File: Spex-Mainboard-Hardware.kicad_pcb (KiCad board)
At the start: 4 copper layers, 82 x 84.7 mm, 118 parts, among them P1 USB_OTG, P13 CONN_01X02, P14 CONN_01X02, P2 SWD Header, P3 CONN_01X04, P4 CONN_01X04, P5 CONN_01X04, P6 CONN_01X04, P7 CONN_01X02, P8 CONN_01X02, P9 CONN_01X02, Q105 Si3407DV, Q106 Q_PNP_BEC, Q3 BSS215PH6327, Q4 Si5468DC, Q5 Si5468DC, Q6 Si5468DC, SW1 SW_PUSH, SW2 SW_PUSH, U1 MKL02Z32VFG4, U10 LM4030, U105 TPS563200, U108 TPS563200, U12 ST1480ABDR, U13 SCHA4B0419, U14 AT45DB641E, U2 NUP2201MR6, U3 MK20DX256VLH7, U4 NUP2201MR6, U5 NUP2201MR6, U6 MMQA6V2T1G, U7 MCP9808T, U8 BME280, U9 LSM9DS1, Y1 Crystal

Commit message: added images
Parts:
- moved C105 99.8 mm to (174.7, 75.8)
- moved C11 99.8 mm to (150.7, 118.3)
- moved C114 99.8 mm to (166.1, 76.0)
- moved C119 99.8 mm to (151.8, 71.8)
- moved C12 99.8 mm to (154.0, 127.9)
- moved C120 99.8 mm to (155.5, 77.4)
- moved C121 99.8 mm to (163.9, 64.4)
- moved C123 99.8 mm to (144.8, 69.2)
- moved C13 99.8 mm to (154.0, 121.4)
- moved C14 99.8 mm to (183.5, 61.1)
- moved C15 99.8 mm to (154.0, 123.6)
- moved C16 99.8 mm to (154.0, 125.3)
- moved C18 99.8 mm to (170.8, 123.7)
- moved C19 99.8 mm to (116.1, 111.6)
- moved C2 99.8 mm to (148.5, 107.1)
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
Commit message: small update
getting ready to order PCB's, making sure they are good to go.
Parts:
- removed P2: SWD Header, SPEX_Parts:SWD-10
- moved P9 4.60 mm to (191.3, 103.1)
- moved Q6 4.60 mm to (179.2, 104.5)
- moved R37 4.60 mm to (175.6, 105.2)
- moved P8 4.47 mm to (191.3, 94.0)
- moved R36 4.47 mm to (175.6, 96.0)
- moved Q5 4.47 mm to (179.2, 95.3)
- moved P7 4.37 mm to (191.3, 84.8)
- moved R35 4.37 mm to (175.6, 86.9)
- moved Q4 4.37 mm to (179.2, 86.2)
- moved P4 1.92 mm to (191.5, 121.2)
- moved P3 1.92 mm to (191.5, 110.1)
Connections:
- net VBatt renamed /Power Distribution/VBat
- P3 pad 2: I2C1_SDA -> I2C1_SCL
- P3 pad 3: I2C1_SCL -> I2C1_SDA
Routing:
- net Vbus_MOS_CTRL: track 23.7 -> 28.8 mm
- net Vbus: track 64.0 -> 69.0 mm
- net I2C1_SDA: track 54.8 -> 57.4 mm
- net UART2_RX: track 51.2 -> 53.4 mm
- net UART2_TX: track 50.7 -> 52.7 mm
- net 5V_MOS_CTRL: track 27.4 -> 28.7 mm
- net 3.3V_MOS_CTRL: track 34.9 -> 36.0 mm
- net GND: track 128.9 -> 129.9 mm, vias 59 -> 60
- net SPI0_SCK: track 69.7 -> 70.5 mm
- net +5V: track 62.5 -> 63.3 mm
- added copper zone on F.Cu, net VBatt
- removed copper zone on F.Cu, net /Power Distribution/VBat

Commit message: small update round 2
cleaning up PCB, adding SPI CS pullup resistors
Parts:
- added R19: 10K, Resistors_SMD:R_0603, F.Cu at (138.5, 127.1)
- added R20: 10K, Resistors_SMD:R_0603, F.Cu at (156.8, 109.6)
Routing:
- net /Power Distribution/VBat: track 0.00 -> 10.9 mm
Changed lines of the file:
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@@
 (kicad_pcb (version 4) (host pcbnew 4.0.2-stable)
   (general
-    (links 336)
+    (links 340)
     (no_connects 20)
     (area 112.379999 54.109999 194.480001 138.910001)
     (thickness 1.6)
     (drawings 4)
-    (tracks 1091)
+    (tracks 1096)
     (zones 0)
-    (modules 117)
+    (modules 119)
     (nets 119)
   )
@@
       (net 2 GND))
   )
+  (module Resistors_SMD:R_0603 (layer F.Cu)
+    (at 138.4561 127.1016)
+    (descr "Resistor SMD 0603, reflow soldering, Vishay (see dcrcw.pdf)")
+    (tags "resistor 0603")
+    (attr smd)
+    (fp_text reference R19 (at -0.623 -1.2446) (layer F.SilkS)
+      (effects (font (size 0.5 0.5) (thickness 0.125)))
+    )
+    (fp_text value 10K (at -0.6357 1.2827) (layer F.Fab)
+      (effects (font (size 0.5 0.5) (thickness 0.125)))
+    )
+    (fp_line (start -1.3 -0.8) (end 1.3 -0.8) (layer F.CrtYd) (width 0.05))
+    (fp_line (start -1.3 0.8) (end 1.3 0.8) (layer F.CrtYd) (width 0.05))
+    (fp_line (start -1.3 -0.8) (end -1.3 0.8) (layer F.CrtYd) (width 0.05))
+    (fp_line (start 1.3 -0.8) (end 1.3 0.8) (layer F.CrtYd) (width 0.05))
+    (fp_line (start 0.5 0.675) (end -0.5 0.675) (layer F.SilkS) (width 0.15))
+    (fp_line (start -0.5 -0.675) (end 0.5 -0.675) (layer F.SilkS) (width 0.15))
+    (pad 1 smd rect (at -0.75 0) (size 0.5 0.9) (layers F.Cu F.Paste F.Mask)
+      (net 1 +3V3))
+    (pad 2 smd rect (at 0.75 0) (size 0.5 0.9) (layers F.Cu F.Paste F.Mask)
+      (net 89 SPI0_CS1))
+    (model Resistors_SMD.3dshapes/R_0603.wrl
+      (at (xyz 0 0 0))
+      (scale (xyz 1 1 1))
+      (rotate (xyz 0 0 0))
+    )
+  )
+  (module Resistors_SMD:R_0603 (layer F.Cu)
+    (at 156.7942 109.5756)
+    (descr "Resistor SMD 0603, reflow soldering, Vishay (see dcrcw.pdf)")
+    (tags "resistor 0603")
+    (attr smd)
+    (fp_text reference R20 (at -0.6731 -1.1811) (layer F.SilkS)
+      (effects (font (size 0.5 0.5) (thickness 0.125)))
+    )
+    (fp_text value 10K (at -0.6223 1.2192) (layer F.Fab)
+      (effects (font (size 0.5 0.5) (thickness 0.125)))
+    )
+    (fp_line (start -1.3 -0.8) (end 1.3 -0.8) (layer F.CrtYd) (width 0.05))
+    (fp_line (start -1.3 0.8) (end 1.3 0.8) (layer F.CrtYd) (width 0.05))
+    (fp_line (start -1.3 -0.8) (end -1.3 0.8) (layer F.CrtYd) (width 0.05))
+    (fp_line (start 1.3 -0.8) (end 1.3 0.8) (layer F.CrtYd) (width 0.05))
+    (fp_line (start 0.5 0.675) (end -0.5 0.675) (layer F.SilkS) (width 0.15))
+    (fp_line (start -0.5 -0.675) (end 0.5 -0.675) (layer F.SilkS) (width 0.15))
+    (pad 1 smd rect (at -0.75 0) (size 0.5 0.9) (layers F.Cu F.Paste F.Mask)
+      (net 1 +3V3))
+    (pad 2 smd rect (at 0.75 0) (size 0.5 0.9) (layers F.Cu F.Paste F.Mask)
+      (net 90 SPI0_CS0))
+    (model Resistors_SMD.3dshapes/R_0603.wrl
+      (at (xyz 0 0 0))
+      (scale (xyz 1 1 1))
+      (rotate (xyz 0 0 0))
+    )
+  )
   (gr_line (start 112.43 54.16) (end 194.43 54.16) (angle 90) (layer Edge.Cuts) (width 0.1))
   (gr_line (start 194.43 54.16) (end 194.43 138.86) (angle 90) (layer Edge.Cuts) (width 0.1))
@@
   (segment (start 140.659699 100.30359) (end 140.603289 100.36) (width 0.2032) (layer B.Cu) (net 117))
   (segment (start 161.04859 100.30359) (end 140.659699 100.30359) (width 0.2032) (layer B.Cu) (net 117))
+  (segment (start 130.8608 67.9831) (end 132.6601 67.9831) (width 0.2032) (layer F.Cu) (net 118))
+  (segment (start 132.6601 67.9831) (end 133.18 67.4632) (width 0.2032) (layer F.Cu) (net 118))
+  (segment (start 133.18 67.4632) (end 133.18 66.11) (width 0.2032) (layer F.Cu) (net 118))
+  (segment (start 128.3339 70.51) (end 130.8608 67.9831) (width 0.2032) (layer F.Cu) (net 118))
+  (segment (start 124.88 70.51) (end 128.3339 70.51) (width 0.2032) (layer F.Cu) (net 118))
   (zone (net 2) (net_name GND) (layer B.Cu) (hatch edge 0.508)
     (connect_pads (clearance 0.25))

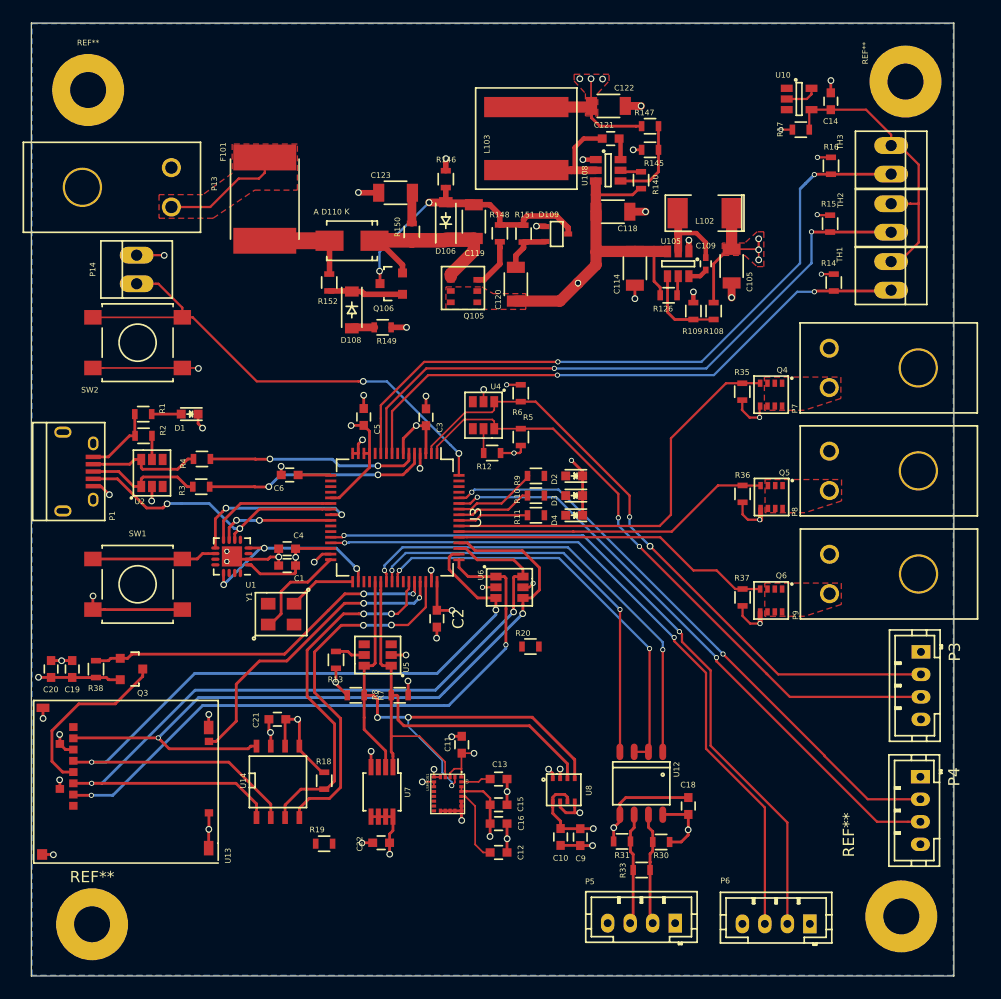
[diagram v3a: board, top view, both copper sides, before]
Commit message: fixed mounting points
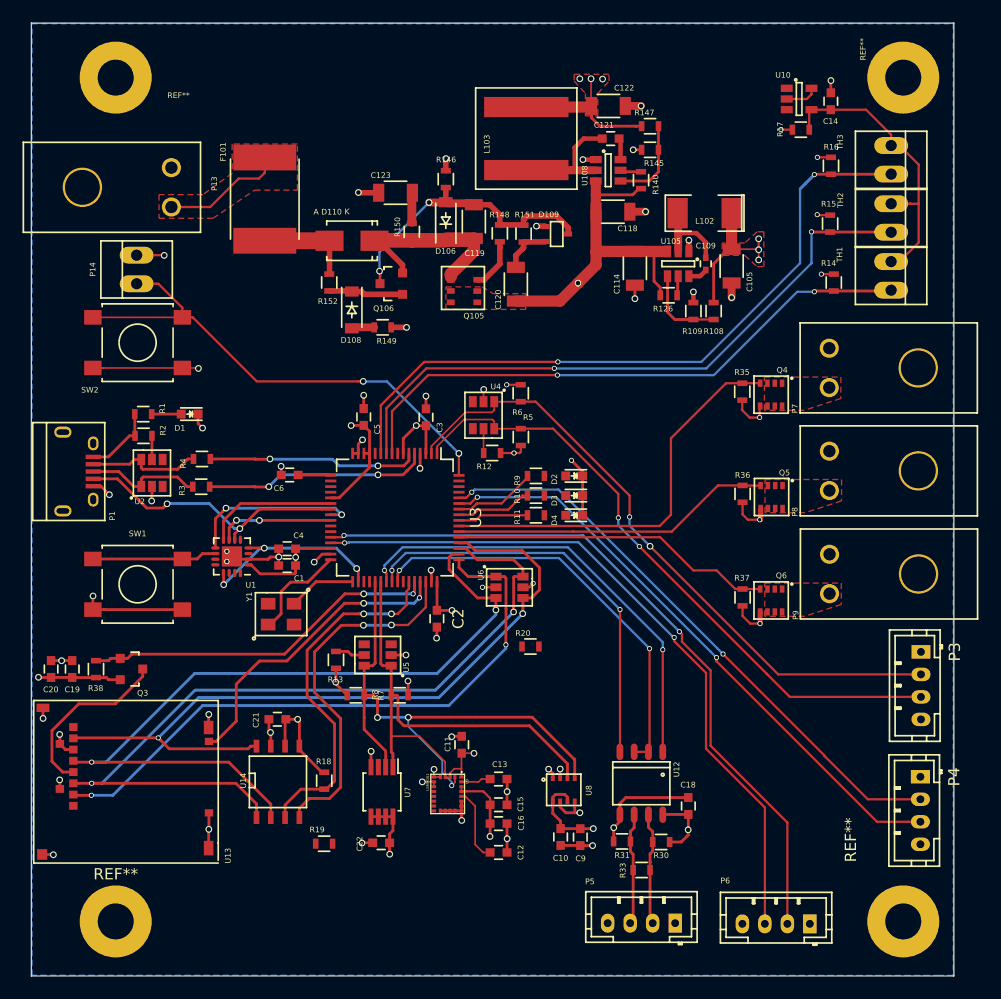
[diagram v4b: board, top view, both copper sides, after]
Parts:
- moved REF** 2.69 mm to (119.9, 59.0)
- moved REF** 2.11 mm to (119.9, 134.0)
- moved REF** 0.48 mm to (189.9, 134.0)
- moved REF** 0.40 mm to (189.9, 59.0)
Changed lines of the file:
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@@
 (kicad_pcb (version 4) (host pcbnew 4.0.2-stable)
   (general
-    (links 340)
-    (no_connects 20)
-    (area 112.379999 54.109999 194.480001 138.910001)
+    (links 324)
+    (no_connects 9)
+    (area 110.8283 54.109999 198.2903 138.910001)
     (thickness 1.6)
     (drawings 4)
@@
   )
   (setup
-    (last_trace_width 0.2032)
+    (last_trace_width 0.254)
     (user_trace_width 0.1524)
     (user_trace_width 0.2032)
@@
     (mod_text_size 1 1)
     (mod_text_width 0.15)
-    (pad_size 1.5 1.5)
-    (pad_drill 0.6)
+    (pad_size 6.4 6.4)
+    (pad_drill 3.2)
     (pad_to_mask_clearance 0)
     (aux_axis_origin 0 0)
@@
     (add_net "Net-(P1-Pad2)")
     (add_net "Net-(P1-Pad3)")
-    (add_net "Net-(P2-Pad6)")
-    (add_net "Net-(P2-Pad7)")
-    (add_net "Net-(P2-Pad8)")
-    (add_net "Net-(P2-Pad9)")
     (add_net "Net-(Q101-Pad3)")
     (add_net "Net-(Q104-Pad3)")
@@
   )
   (module Mounting_Holes:MountingHole_3.2mm_M3_Pad (layer F.Cu)
-    (at 117.83 134.26)
+    (at 119.93 134.01)
     (descr "Mounting Hole 3.2mm, M3")
     (tags "mounting hole 3.2mm m3")
@@
   )
   (module Mounting_Holes:MountingHole_3.2mm_M3_Pad (layer F.Cu)
-    (at 117.48 60.11)
+    (at 119.93 59.01)
     (descr "Mounting Hole 3.2mm, M3")
     (tags "mounting hole 3.2mm m3")
-    (fp_text reference REF** (at 0 -4.2) (layer F.SilkS)
+    (fp_text reference REF** (at 5.5841 1.5817) (layer F.SilkS)
       (effects (font (size 0.5 0.5) (thickness 0.125)))
     )
-    (fp_text value MountingHole_3.2mm_M3_Pad (at 1.302 -5.178) (layer F.Fab)
+    (fp_text value MountingHole_3.2mm_M3_Pad (at -0.0293 -4.0952) (layer F.Fab)
       (effects (font (size 0.5 0.5) (thickness 0.125)))
     )
@@
   )
   (module Mounting_Holes:MountingHole_3.2mm_M3_Pad (layer F.Cu)
-    (at 190.13 59.36)
+    (at 189.93 59.01)
     (descr "Mounting Hole 3.2mm, M3")
     (tags "mounting hole 3.2mm m3")
@@
   )
   (module Mounting_Holes:MountingHole_3.2mm_M3_Pad (layer F.Cu)
-    (at 189.755 133.56)
+    (at 189.93 134.01)
     (descr "Mounting Hole 3.2mm, M3")
     (tags "mounting hole 3.2mm m3")
@@
       (effects (font (size 1 1) (thickness 0.15)))
     )
-    (fp_text value MountingHole_3.2mm_M3_Pad (at -1.377 4.43) (layer F.Fab)
+    (fp_text value MountingHole_3.2mm_M3_Pad (at -1.6779 3.9247) (layer F.Fab)
       (effects (font (size 0.5 0.5) (thickness 0.125)))
     )
@@
     (connect_pads (clearance 0.25))
     (min_thickness 0.254)
-    (fill (arc_segments 16) (thermal_gap 0.508) (thermal_bridge_width 0.508))
+    (fill yes (arc_segments 16) (thermal_gap 0.508) (thermal_bridge_width 0.508))
     (polygon
       (pts

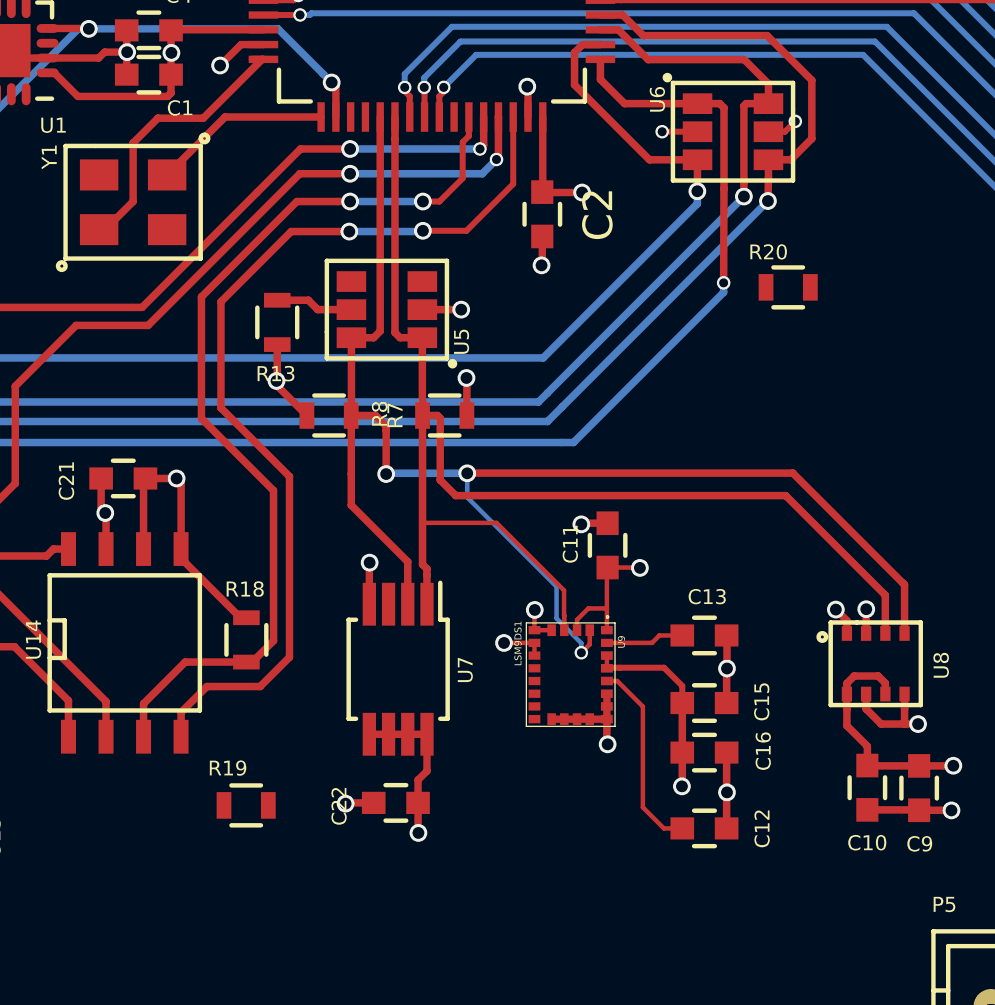
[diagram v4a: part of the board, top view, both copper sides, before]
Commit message: routed SPI CS pull up resistors
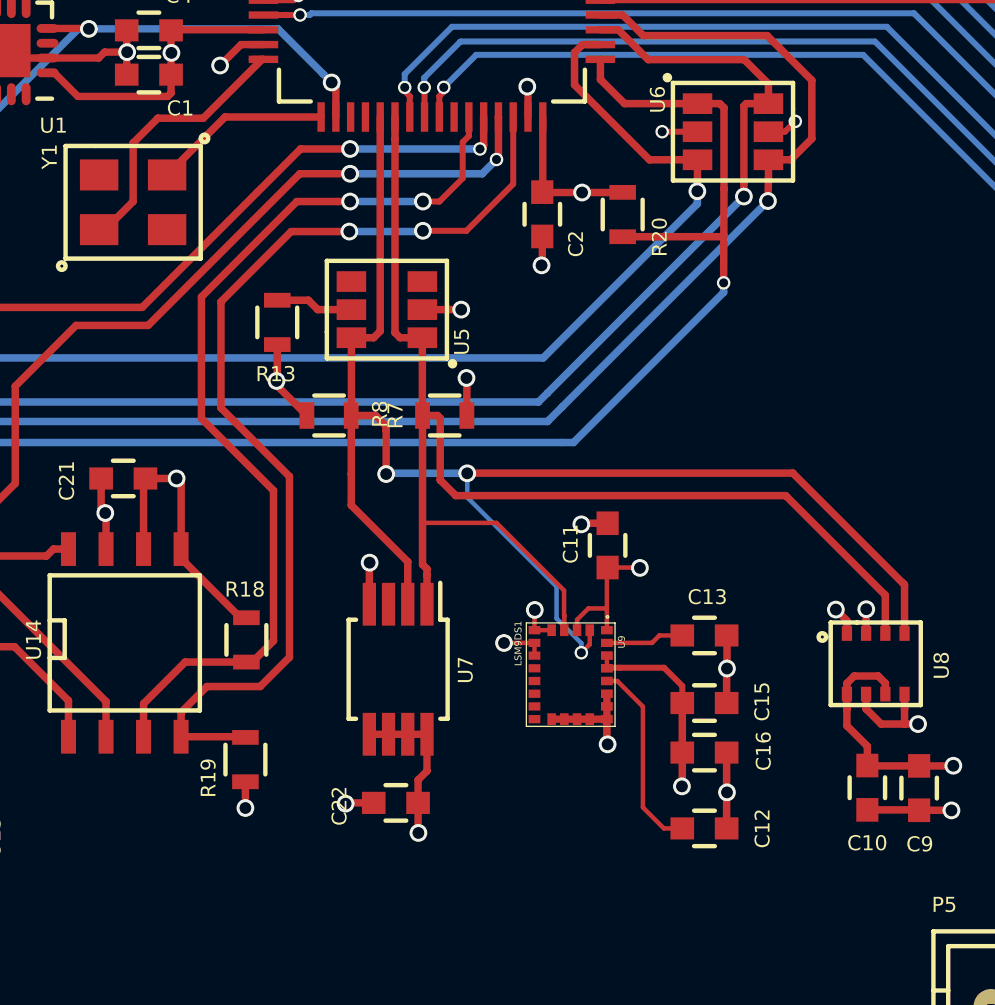
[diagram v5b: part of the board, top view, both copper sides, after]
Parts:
- moved R20 6.12 mm to (151.2, 107.1), turned to 270 degrees
- moved R19 1.55 mm to (138.4, 125.6), turned to 90 degrees
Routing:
- net SPI0_CS0: track 55.4 -> 58.8 mm
- net +3V3: track 101.9 -> 104.1 mm, vias 21 -> 22
- net SPI0_CS1: track 32.1 -> 34.2 mm
- added copper zone on F.Cu, net /Power Distribution/VBat
- removed copper zone on F.Cu, net VBatt

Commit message: small tweaks, BOM updated
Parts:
- added R21: 50K, Resistors_SMD:R_0603, F.Cu at (124.0, 112.6)
- added R22: 50K, Resistors_SMD:R_0603, F.Cu at (126.2, 130.1)
- moved R20 2.74 mm to (153.8, 107.8), turned to 0 degrees
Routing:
- net Net-(R22-Pad1): track 0.00 -> 11.9 mm
- net Net-(R21-Pad2): track 0.00 -> 9.56 mm
- net +3V3: track 104.1 -> 108.8 mm, vias 22 -> 24
- net SPI0_CS0: track 58.8 -> 55.2 mm
- net Vbus: track 69.0 -> 71.0 mm
- net /PTB1: track 15.4 -> 16.1 mm

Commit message: Continued tweaks, updated BOM again
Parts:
- R21, R22: value 50K -> 51K
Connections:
- U10 pad 2: Net-(U10-Pad2) -> GND
- U10 pad 5: Net-(U10-Pad2) -> GND
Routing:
- net Net-(C119-Pad1): track 17.7 -> 24.7 mm
- net GND: track 130.3 -> 134.8 mm
- net Net-(U10-Pad2): track 2.90 -> 0.00 mm
